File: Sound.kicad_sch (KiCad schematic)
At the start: 2 parts, among them U4 X1000

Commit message: Update (Display)
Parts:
- U4: footprint (none) -> TheBrutzlers_Lib:BGA256C80P16X16_1300X1300X130N
- renumbered C73 to C74
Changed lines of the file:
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@@
     (property "Reference" "U4" (id 0) (at 135.89 39.37 0))
     (property "Value" "X1000" (id 1) (at 135.89 41.91 0))
-    (property "Footprint" "" (id 2) (at 138.43 57.15 0)
+    (property "Footprint" "TheBrutzlers_Lib:BGA256C80P16X16_1300X1300X130N" (id 2) (at 138.43 57.15 0)
       (effects (font (size 1.27 1.27)) (justify left) hide)
     )
@@
   (symbol (lib_id "Device:C") (at 167.64 53.34 0) (unit 1)
     (in_bom yes) (on_board yes) (fields_autoplaced)
-    (property "Reference" "C73" (id 0) (at 171.45 52.0699 0)
+    (property "Reference" "C74" (id 0) (at 171.45 52.0699 0)
       (effects (font (size 1.27 1.27)) (justify left))
     )

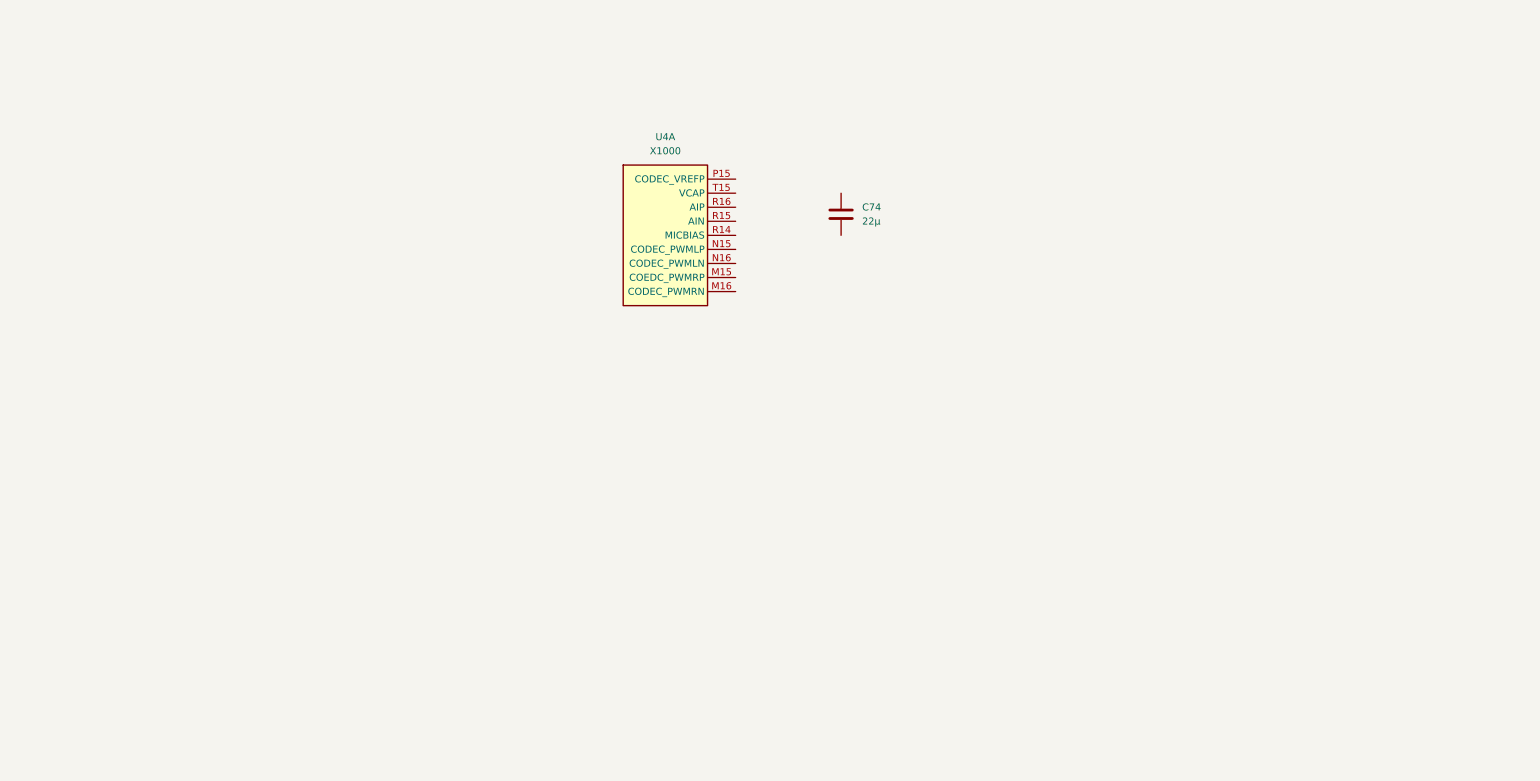
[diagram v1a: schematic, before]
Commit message: Add Audio
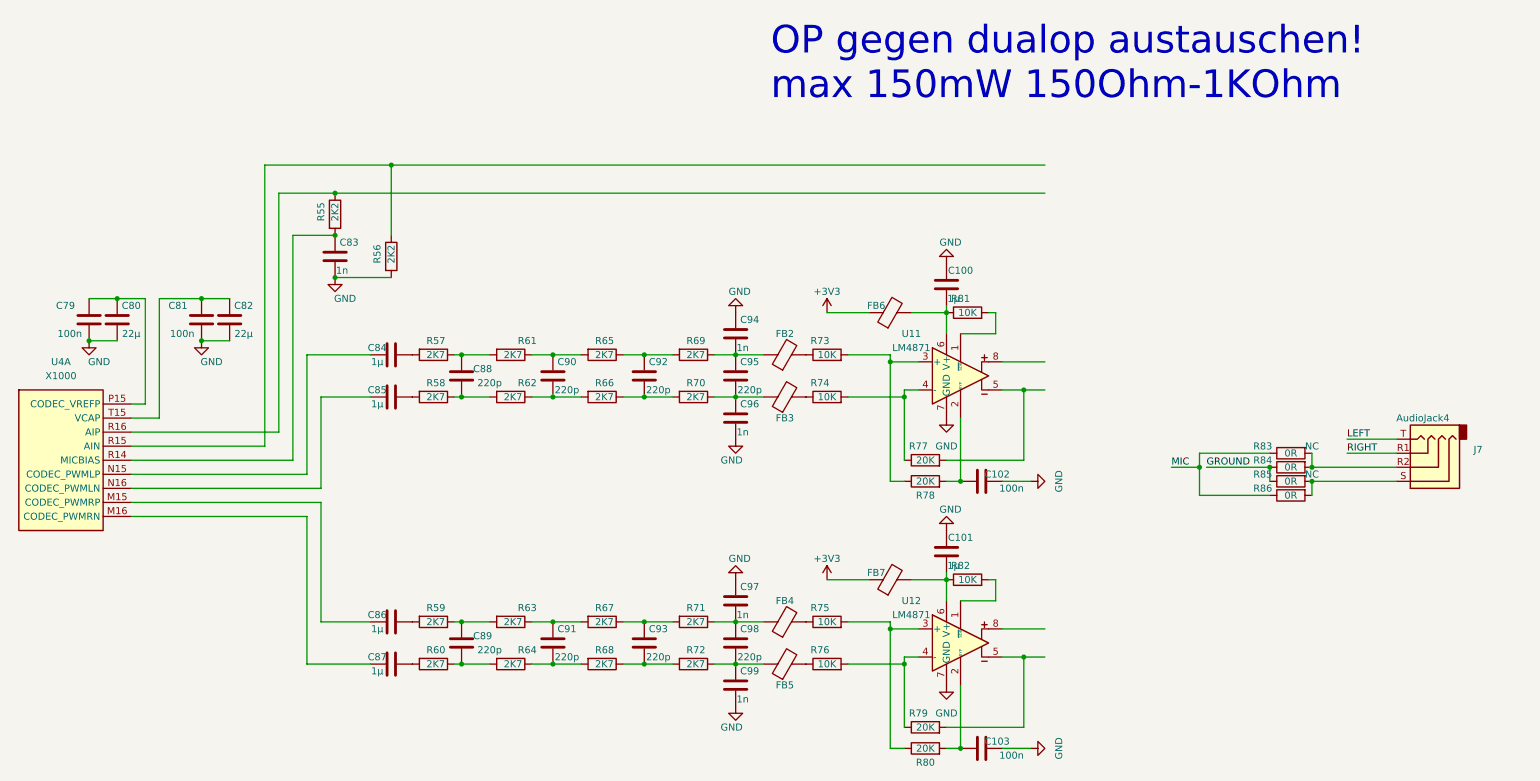
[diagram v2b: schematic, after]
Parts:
- removed C74: 22µ, Capacitor_SMD:C_0603_1608Metric, symbol Device:C
- added C100, C101, C84, C85, C86, C87: 1µ, Capacitor_SMD:C_0402_1005Metric, symbol Device:C
- added C102, C103, C79, C81: 100n, Capacitor_SMD:C_0402_1005Metric, symbol Device:C
- added C80, C82: 22µ, Capacitor_SMD:C_0603_1608Metric, symbol Device:C
- added C83, C94, C96, C97, C99: 1n, Capacitor_SMD:C_0402_1005Metric, symbol Device:C
- added C88, C89, C90, C91, C92, C93, C95, C98: 220p, Capacitor_SMD:C_0402_1005Metric, symbol Device:C
- added FB2, FB3, FB4, FB5, FB6, FB7: FerriteBead, Resistor_SMD:R_0402_1005Metric, symbol Device:FerriteBead
- added J7: AudioJack4, TheBrutzlers_Lib:AUDIO_3.5mm_PJ-313B6-B, symbol Connector:AudioJack4
- added R55, R56: 2K2, Resistor_SMD:R_0402_1005Metric, symbol Device:R
- added R57, R58, R59, R60, R61, R62, R63, R64, R65, R66, R67, R68, R69, R70, R71, R72: 2K7, Resistor_SMD:R_0402_1005Metric, symbol Device:R
- added R73, R74, R75, R76, R81, R82: 10K, Resistor_SMD:R_0402_1005Metric, symbol Device:R
- added R77, R78, R79, R80: 20K, Resistor_SMD:R_0402_1005Metric, symbol Device:R
- added R83, R84, R85, R86: 0R, Resistor_SMD:R_0402_1005Metric, symbol Device:R
- added U11, U12: LM4871, Package_SO:SOIC-8_3.9x4.9mm_P1.27mm, symbol Amplifier_Audio:IS31AP4991-SLS2
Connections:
- net at U4.M15 (CODEC_PWMRP): now also C86.1
- net at U4.M16 (CODEC_PWMRN): now also C87.1
- net at U4.N15 (CODEC_PWMLP): now also C84.1
- net at U4.N16 (CODEC_PWMLN): now also C85.1
- net at U4.P15 (CODEC_VREFP): now also C79.2, C80.2
- net at U4.R14 (MICBIAS): now also C83.1, R55.2
- net at U4.R15 (AIN): now also R56.1
- net at U4.R16 (AIP): now also R55.1
- net at U4.T15 (VCAP): now also C81.2, C82.2
- new net: J7.R2, R83.2, R84.2
- new net: C100.2, FB6.2, R81.1, U11.6 (V+)
- new net: R81.2, U11.1 (~{SDB})
- new net: C101.2, FB7.2, R82.1, U12.6 (V+)
- new net: C92.1, R65.1, R69.2
- new net: C92.2, R66.1, R70.2
- new net: C90.1, R61.1, R65.2
- new net: C88.1, R57.1, R61.2
- new net: FB3.2, R74.1
- new net: R74.2, R77.1, U11.4 (-)
- new net: C84.2, R57.2
- new net: C91.1, R63.1, R67.2
- new net: C89.1, R59.1, R63.2
- new net: R82.2, U12.1 (~{SDB})
- new net: C88.2, R58.1, R62.2
- new net: J7.S, R85.2, R86.2
- new net: C95.2, C96.1, FB3.1, R70.1
- new net: C93.1, R67.1, R71.2
- new net: C93.2, R68.1, R72.2
- new net: C97.2, C98.1, FB4.1, R71.1
- new net: C94.2, C95.1, FB2.1, R69.1
- new net: C85.2, R58.2
- new net: C98.2, C99.1, FB5.1, R72.1
- new net: FB5.2, R76.1
- new net: C103.1, R80.2, U12.2 (BYP)
- new net: FB4.2, R75.1
- new net: C89.2, R60.1, R64.2
- new net: C87.2, R60.2
- new net: R75.2, R80.1, U12.3 (+)
- new net: C91.2, R64.1, R68.2
- new net: R76.2, R79.1, U12.4 (-)
- new net: R79.2, U12.5
- new net: FB2.2, R73.1
- new net: R73.2, R78.1, U11.3 (+)
- new net: C102.1, R78.2, U11.2 (BYP)
- new net: C86.2, R59.2
- new net: C90.2, R62.1, R66.2
- new net: R77.2, U11.5
- new net +3V3: FB6.1, FB7.1
- new net GND: C100.1, C101.1, C102.2, C103.2, C79.1, C80.1, C81.1, C82.1, C83.2, C94.1, C96.2, C97.1, C99.2, R56.2, U11.7 (GND), U12.7 (GND)
- new net GROUND: R84.1, R85.1
- new net LEFT: J7.T
- new net MIC: R83.1, R86.1
- new net RIGHT: J7.R1
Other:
- note added: "OP gegen dualop austauschen! max 150mW 150Ohm-1KOhm"

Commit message: Display Update
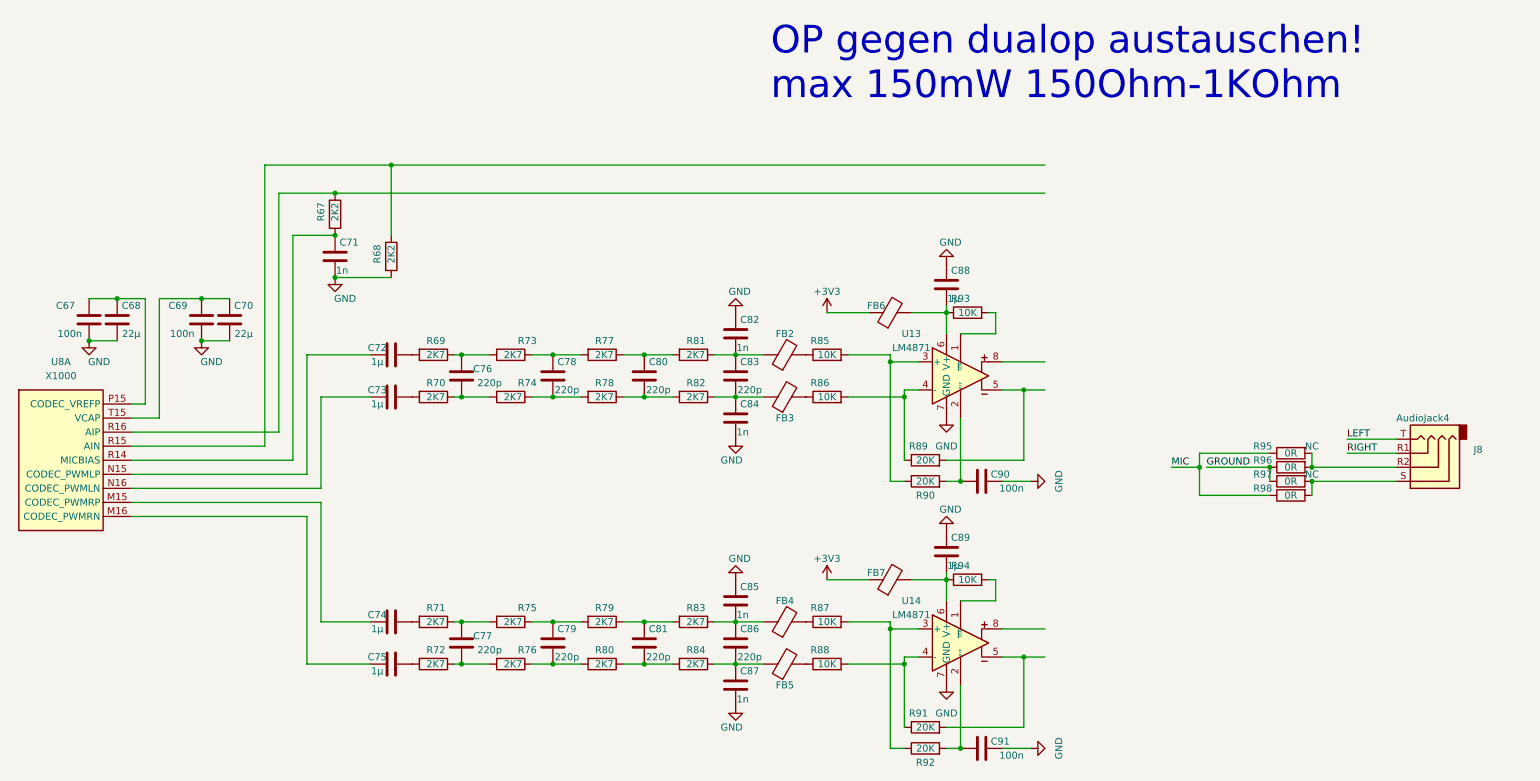
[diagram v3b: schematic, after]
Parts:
- renumbered C79 to C67, C80 to C68, C81 to C69, C82 to C70, C83 to C71, C84 to C72, C85 to C73, C86 to C74, C87 to C75, C88 to C76, C89 to C77, C90 to C78, C91 to C79, C92 to C80, C93 to C81, C94 to C82, C95 to C83, C96 to C84, C97 to C85, C98 to C86, C99 to C87, C100 to C88, C101 to C89, C102 to C90, C103 to C91, J7 to J8, R55 to R67, R56 to R68, R57 to R69, R58 to R70, R59 to R71, R60 to R72, R61 to R73, R62 to R74, R63 to R75, R64 to R76, R65 to R77, R66 to R78, R67 to R79, R68 to R80, R69 to R81, R70 to R82, R71 to R83, R72 to R84, R73 to R85, R74 to R86, R75 to R87, R76 to R88, R77 to R89, R78 to R90, R79 to R91, R80 to R92, R81 to R93, R82 to R94, R83 to R95, R84 to R96, R85 to R97, R86 to R98, U11 to U13, U12 to U14, U4 to U8

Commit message: update DDR
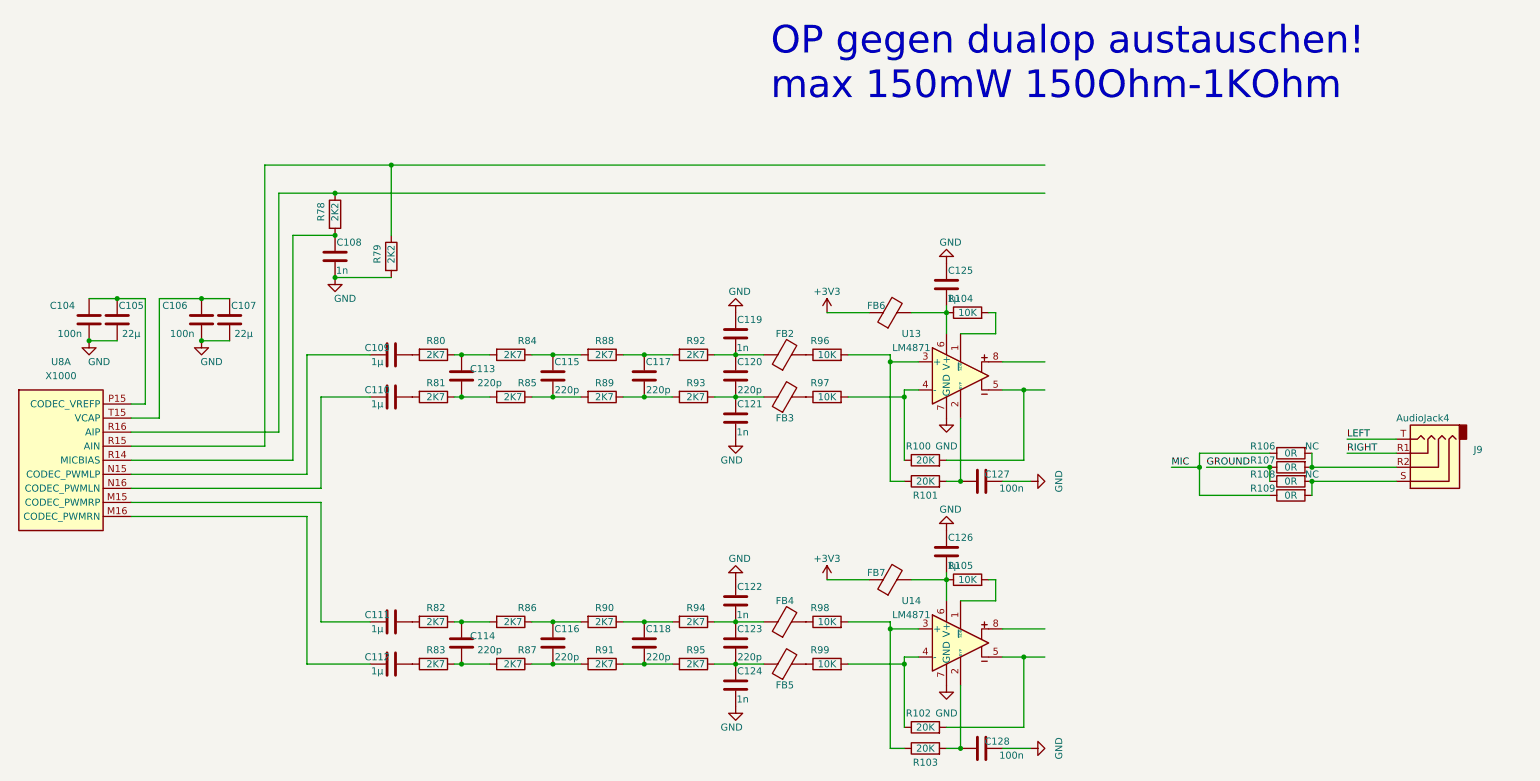
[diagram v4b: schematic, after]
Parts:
- renumbered C67 to C104, C68 to C105, C69 to C106, C70 to C107, C71 to C108, C72 to C109, C73 to C110, C74 to C111, C75 to C112, C76 to C113, C77 to C114, C78 to C115, C79 to C116, C80 to C117, C81 to C118, C82 to C119, C83 to C120, C84 to C121, C85 to C122, C86 to C123, C87 to C124, C88 to C125, C89 to C126, C90 to C127, C91 to C128, J8 to J9, R89 to R100, R90 to R101, R91 to R102, R92 to R103, R93 to R104, R94 to R105, R95 to R106, R96 to R107, R97 to R108, R98 to R109, R67 to R78, R68 to R79, R69 to R80, R70 to R81, R71 to R82, R72 to R83, R73 to R84, R74 to R85, R75 to R86, R76 to R87, R77 to R88, R78 to R89, R79 to R90, R80 to R91, R81 to R92, R82 to R93, R83 to R94, R84 to R95, R85 to R96, R86 to R97, R87 to R98, R88 to R99
